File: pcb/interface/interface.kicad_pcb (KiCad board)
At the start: 2 copper layers, 51.5 x 25 mm, 36 parts, among them J1 SEGMENTS, J16 BUS_IN, J17 BUS_OUT, J5 SELECT, Q1 MMBT3904, Q2 MMBT3904, Q3 MMBT3904, Q4 MMBT3904, U1 74HC595, U2 74HC595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

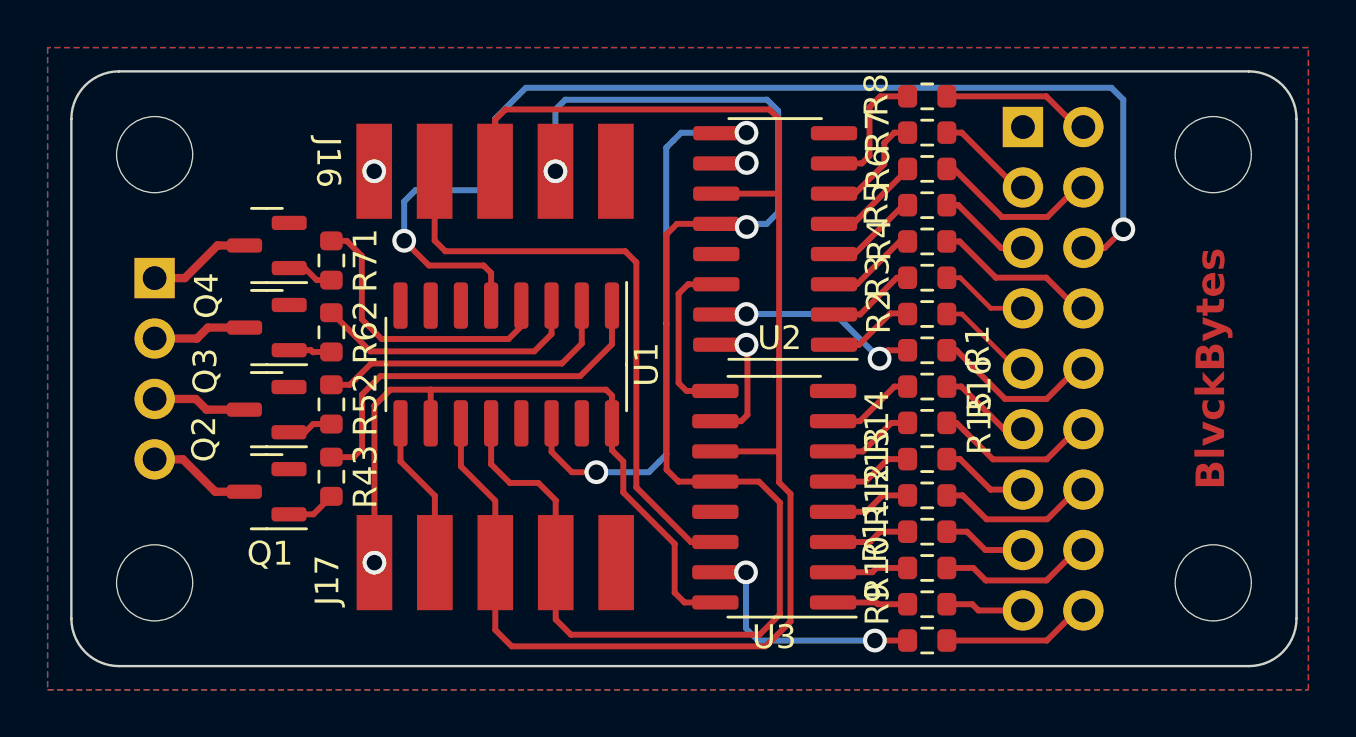
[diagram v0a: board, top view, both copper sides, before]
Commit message: added missing input pulldown resistors to the interface board
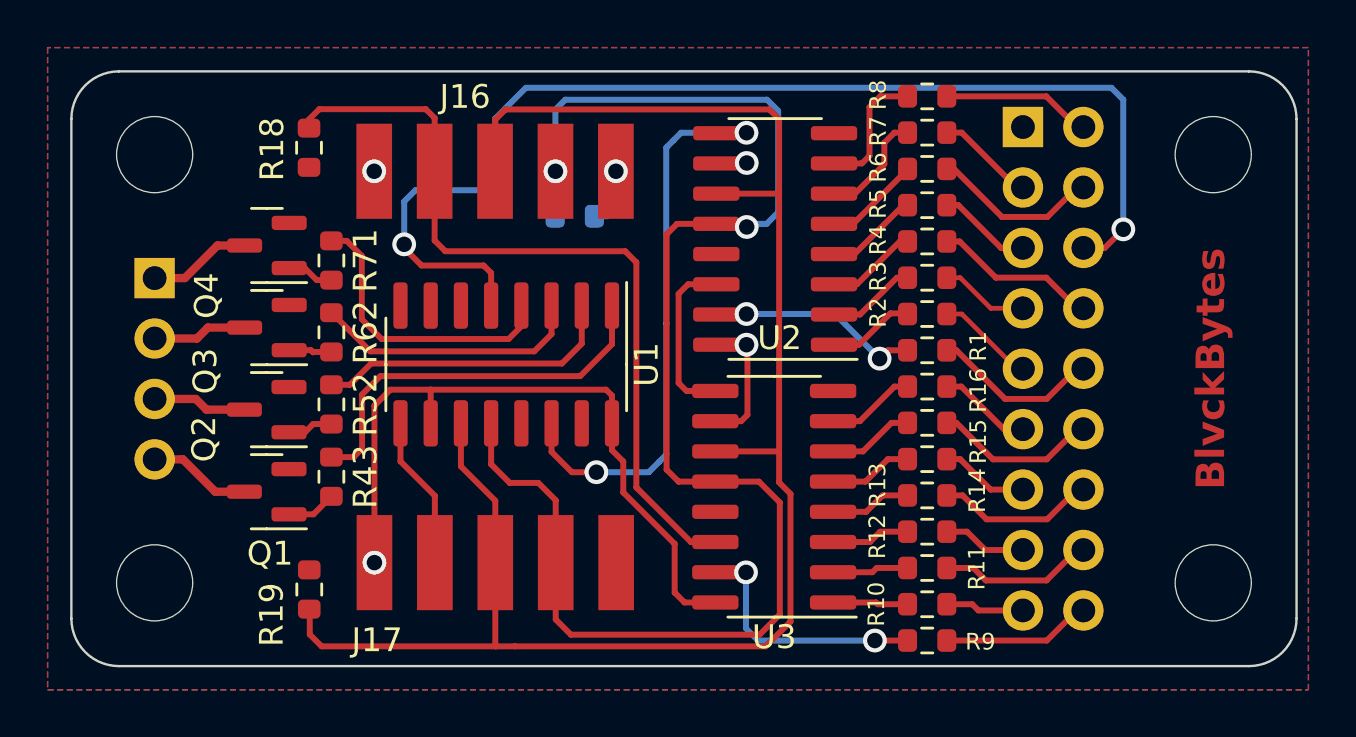
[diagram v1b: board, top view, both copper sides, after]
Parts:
- added R18: 10k, Resistor_SMD:R_0603_1608Metric, F.Cu at (122.0, 101.7)
- added R19: 10k, Resistor_SMD:R_0603_1608Metric, F.Cu at (122.0, 120.3)
- added R20: 10k, Resistor_SMD:R_0603_1608Metric, B.Cu at (133.2, 104.6)
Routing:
- net SRCLK: track 63.6 -> 73.1 mm
- net SER_IN: track 25.4 -> 33.7 mm
- net GND: track 0.00 -> 2.57 mm, vias 0 -> 1
- net RCLK: track 61.6 -> 63.5 mm
